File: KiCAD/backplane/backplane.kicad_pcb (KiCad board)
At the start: 2 copper layers, 121.9 x 88.9 mm, 37 parts, among them P1 CONN_02X04, P10 CONN_02X04, P11 CONN_01X09, P12 CONN_02X04, P13 CONN_01X09, P14 CONN_01X10, P15 CONN_01X10, P16 CONN_02X04, P17 CONN_02X04, P18 CONN_02X04, P19 CONN_01X09, P2 CONN_01X17, P20 CONN_01X04, P21 CONN_01X02, P22 CONN_01X02, P23 CONN_01X02, P3 CONN_01X17, P4 CONN_01X04, P5 CONN_01X09, P6 CONN_02X04, P7 CONN_01X10, P8 CONN_01X10, P9 CONN_02X04, U1 ARDUINO_MICRO

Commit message: switch adapter board mounting
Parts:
- added P24: CONN_01X01, myparts:4994-0-15-15-11-27-10-0, F.Cu at (28.5, -54.6)
- added P25: CONN_01X01, myparts:4994-0-15-15-11-27-10-0, F.Cu at (28.5, -52.1)
- added P26: CONN_01X01, myparts:4994-0-15-15-11-27-10-0, F.Cu at (28.5, -49.5)
- added P27: CONN_01X01, myparts:4994-0-15-15-11-27-10-0, F.Cu at (28.5, -47.0)
- added P28: CONN_01X01, myparts:4994-0-15-15-11-27-10-0, F.Cu at (28.5, -44.5)
- added P29: CONN_01X01, myparts:4994-0-15-15-11-27-10-0, F.Cu at (28.5, -41.9)
- added P30: CONN_01X01, myparts:4994-0-15-15-11-27-10-0, F.Cu at (28.5, -39.4)
- added P31: CONN_01X01, myparts:4994-0-15-15-11-27-10-0, F.Cu at (28.5, -36.8)
- added P32: CONN_01X01, myparts:4994-0-15-15-11-27-10-0, F.Cu at (28.5, -34.3)
- added P33: CONN_01X01, myparts:4994-0-15-15-11-27-10-0, F.Cu at (56.0, -52.1)
- added P34: CONN_01X01, myparts:4994-0-15-15-11-27-10-0, F.Cu at (56.0, -39.4)
- added P35: CONN_01X01, myparts:4994-0-15-15-11-27-10-0, F.Cu at (56.0, -47.0)
- added P36: CONN_01X01, myparts:4994-0-15-15-11-27-10-0, F.Cu at (56.0, -49.5)
- added P37: CONN_01X01, myparts:4994-0-15-15-11-27-10-0, F.Cu at (56.0, -41.9)
- added P38: CONN_01X01, myparts:4994-0-15-15-11-27-10-0, F.Cu at (96.0, -44.5)
- added P39: CONN_01X01, myparts:4994-0-15-15-11-27-10-0, F.Cu at (68.5, -44.5)
- added P40: CONN_01X01, myparts:4994-0-15-15-11-27-10-0, F.Cu at (56.0, -34.3)
- added P41: CONN_01X01, myparts:4994-0-15-15-11-27-10-0, F.Cu at (68.5, -54.6)
- added P42: CONN_01X01, myparts:4994-0-15-15-11-27-10-0, F.Cu at (68.5, -52.1)
- added P43: CONN_01X01, myparts:4994-0-15-15-11-27-10-0, F.Cu at (68.5, -49.5)
- added P44: CONN_01X01, myparts:4994-0-15-15-11-27-10-0, F.Cu at (68.5, -47.0)
- added P45: CONN_01X01, myparts:4994-0-15-15-11-27-10-0, F.Cu at (68.5, -39.4)
- added P46: CONN_01X01, myparts:4994-0-15-15-11-27-10-0, F.Cu at (68.5, -41.9)
- added P47: CONN_01X01, myparts:4994-0-15-15-11-27-10-0, F.Cu at (96.0, -49.5)
- added P48: CONN_01X01, myparts:4994-0-15-15-11-27-10-0, F.Cu at (68.5, -36.8)
- added P49: CONN_01X01, myparts:4994-0-15-15-11-27-10-0, F.Cu at (68.5, -34.3)
- added P50: CONN_01X01, myparts:4994-0-15-15-11-27-10-0, F.Cu at (56.0, -54.6)
- added P51: CONN_01X01, myparts:4994-0-15-15-11-27-10-0, F.Cu at (96.0, -52.1)
- added P52: CONN_01X01, myparts:4994-0-15-15-11-27-10-0, F.Cu at (96.0, -39.4)
- added P53: CONN_01X01, myparts:4994-0-15-15-11-27-10-0, F.Cu at (96.0, -47.0)
- added P54: CONN_01X01, myparts:4994-0-15-15-11-27-10-0, F.Cu at (96.0, -36.8)
- added P55: CONN_01X01, myparts:4994-0-15-15-11-27-10-0, F.Cu at (96.0, -41.9)
- added P56: CONN_01X01, myparts:4994-0-15-15-11-27-10-0, F.Cu at (56.0, -44.5)
- added P57: CONN_01X01, myparts:4994-0-15-15-11-27-10-0, F.Cu at (56.0, -36.8)
- added P58: CONN_01X01, myparts:4994-0-15-15-11-27-10-0, F.Cu at (96.0, -34.3)
- added P59: CONN_01X01, myparts:4994-0-15-15-11-27-10-0, F.Cu at (38.4, -30.7)
- added P60: CONN_01X01, myparts:4994-0-15-15-11-27-10-0, F.Cu at (41.0, -58.2)
- added P61: CONN_01X01, myparts:4994-0-15-15-11-27-10-0, F.Cu at (41.0, -30.7)
- added P62: CONN_01X01, myparts:4994-0-15-15-11-27-10-0, F.Cu at (43.5, -58.2)
- added P63: CONN_01X01, myparts:4994-0-15-15-11-27-10-0, F.Cu at (43.5, -30.7)
- added P64: CONN_01X01, myparts:4994-0-15-15-11-27-10-0, F.Cu at (88.6, -58.2)
- added P65: CONN_01X01, myparts:4994-0-15-15-11-27-10-0, F.Cu at (46.0, -30.7)
- added P66: CONN_01X01, myparts:4994-0-15-15-11-27-10-0, F.Cu at (46.0, -58.2)
- added P67: CONN_01X01, myparts:4994-0-15-15-11-27-10-0, F.Cu at (48.6, -30.7)
- added P68: CONN_01X01, myparts:4994-0-15-15-11-27-10-0, F.Cu at (51.1, -58.2)
- added P69: CONN_01X01, myparts:4994-0-15-15-11-27-10-0, F.Cu at (51.1, -30.7)
- added P70: CONN_01X01, myparts:4994-0-15-15-11-27-10-0, F.Cu at (53.7, -58.2)
- added P71: CONN_01X01, myparts:4994-0-15-15-11-27-10-0, F.Cu at (53.7, -30.7)
- added P72: CONN_01X01, myparts:4994-0-15-15-11-27-10-0, F.Cu at (70.8, -58.2)
- added P73: CONN_01X01, myparts:4994-0-15-15-11-27-10-0, F.Cu at (70.8, -30.7)
- added P74: CONN_01X01, myparts:4994-0-15-15-11-27-10-0, F.Cu at (73.3, -58.2)
- added P75: CONN_01X01, myparts:4994-0-15-15-11-27-10-0, F.Cu at (73.3, -30.7)
- added P76: CONN_01X01, myparts:4994-0-15-15-11-27-10-0, F.Cu at (75.9, -58.2)
- added P77: CONN_01X01, myparts:4994-0-15-15-11-27-10-0, F.Cu at (75.9, -30.7)
- added P78: CONN_01X01, myparts:4994-0-15-15-11-27-10-0, F.Cu at (86.0, -58.2)
- added P79: CONN_01X01, myparts:4994-0-15-15-11-27-10-0, F.Cu at (78.4, -30.7)
- added P80: CONN_01X01, myparts:4994-0-15-15-11-27-10-0, F.Cu at (81.0, -58.2)
- added P81: CONN_01X01, myparts:4994-0-15-15-11-27-10-0, F.Cu at (81.0, -30.7)
- added P82: CONN_01X01, myparts:4994-0-15-15-11-27-10-0, F.Cu at (83.5, -58.2)
- added P83: CONN_01X01, myparts:4994-0-15-15-11-27-10-0, F.Cu at (83.5, -30.7)
- added P84: CONN_01X01, myparts:4994-0-15-15-11-27-10-0, F.Cu at (38.4, -58.2)
- added P85: CONN_01X01, myparts:4994-0-15-15-11-27-10-0, F.Cu at (86.0, -30.7)
- added P86: CONN_01X01, myparts:4994-0-15-15-11-27-10-0, F.Cu at (35.9, -58.2)
- added P87: CONN_01X01, myparts:4994-0-15-15-11-27-10-0, F.Cu at (88.6, -30.7)
- added P88: CONN_01X01, myparts:4994-0-15-15-11-27-10-0, F.Cu at (91.1, -58.2)
- added P89: CONN_01X01, myparts:4994-0-15-15-11-27-10-0, F.Cu at (91.1, -30.7)
- added P90: CONN_01X01, myparts:4994-0-15-15-11-27-10-0, F.Cu at (93.7, -58.2)
- added P91: CONN_01X01, myparts:4994-0-15-15-11-27-10-0, F.Cu at (93.7, -30.7)
- P11, P13, P19, P5: value CONN_01X09 -> CONN_01X01; footprint Socket_Strips:Socket_Strip_Straight_1x09 -> myparts:4994-0-15-15-11-27-10-0
- P14, P15, P7, P8: value CONN_01X10 -> CONN_01X01; footprint Socket_Strips:Socket_Strip_Straight_1x10 -> myparts:4994-0-15-15-11-27-10-0
- moved P13 67.5 mm to (96.0, -54.6), turned to 90 degrees
- moved P11 67.0 mm to (33.3, -30.7), turned to 0 degrees
- moved P7 48.5 mm to (30.8, -30.7)
- moved P8 46.4 mm to (33.3, -58.2)
- moved P5 37.9 mm to (30.8, -58.2), turned to 0 degrees
- moved P19 22.7 mm to (78.4, -58.2), turned to 0 degrees
- moved P14 17.8 mm to (48.6, -58.2)
- moved P15 5.08 mm to (35.9, -30.7)
- renumbered JTAG to CON1
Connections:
- P11 pad 1: +5V -> B1_V
- P13 pad 1: MOSI -> +5V
- P14 pad 1: B0_I -> (no net)
- P15 pad 1: B1_I -> B_I+
- P19 pad 1: +5V -> (no net)
- P5 pad 1: MOSI -> B0_I
- P7 pad 1: A0_I -> B1_I
- P8 pad 1: A1_I -> B0_V
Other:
- board text added: "JTAG"

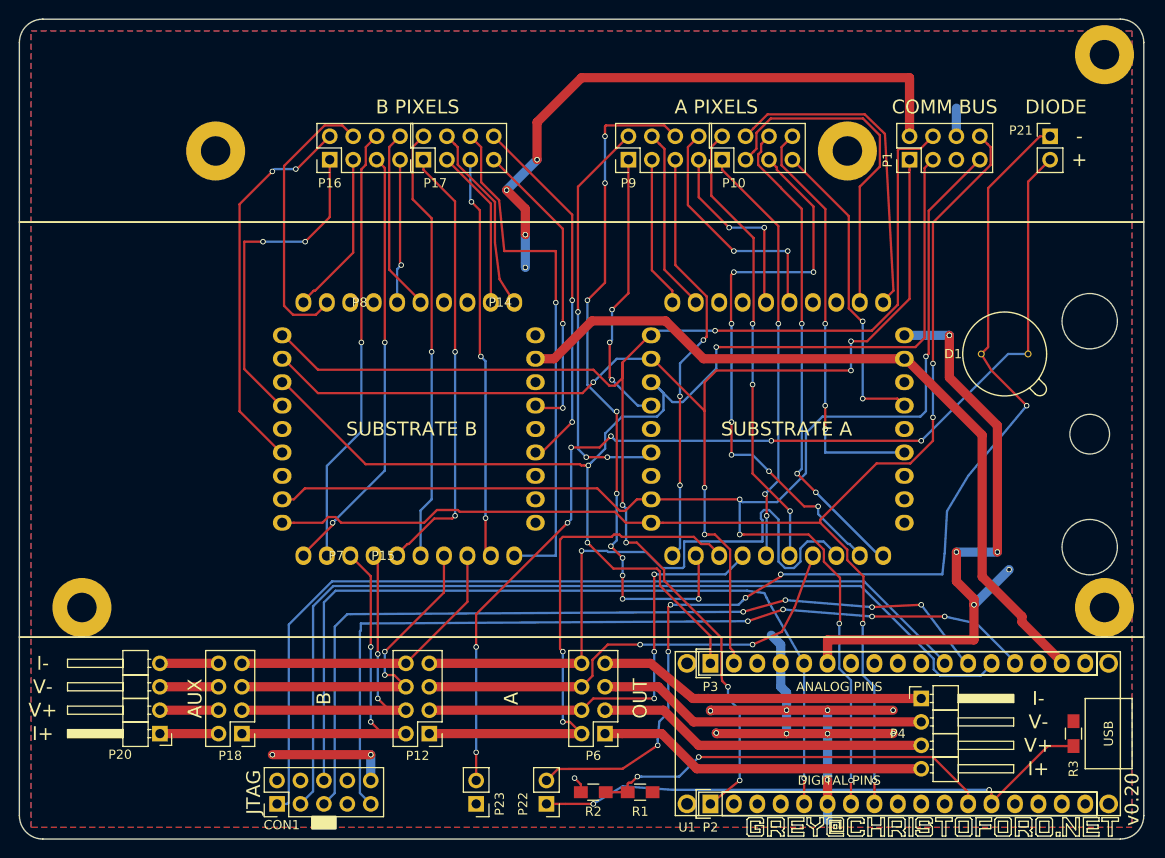
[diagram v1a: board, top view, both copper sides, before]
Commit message: properly link mounting holes to schematic
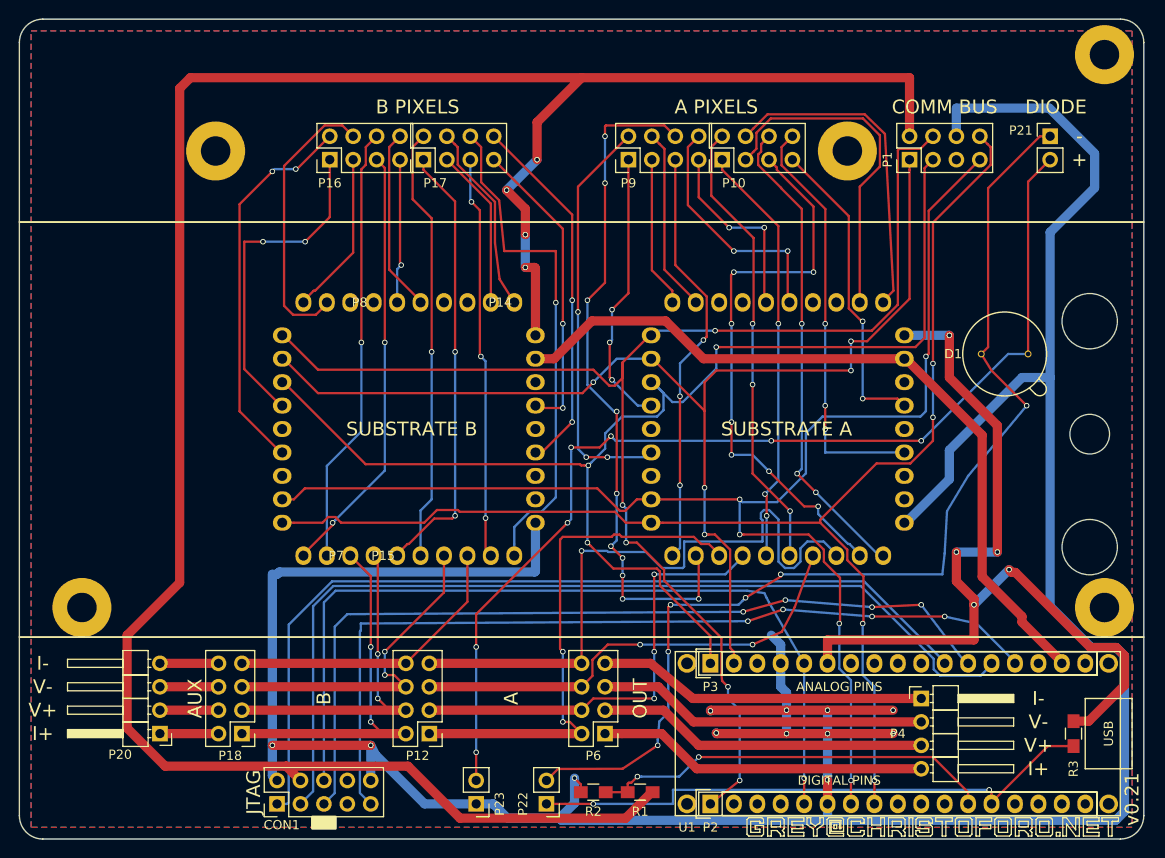
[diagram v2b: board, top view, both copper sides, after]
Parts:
- P92, P96, P97, P98, P99: renamed from REF**; value MountingHole_3.2mm_M3_Pad -> CONN_01X01
- P93, P95: renamed from REF**; value MountingHole_6mm -> CONN_01X01
- P94: renamed from REF**; value MountingHole_4.3mm_M4 -> CONN_01X01
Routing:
- net GND: track 81.0 -> 348.7 mm
- net +5V: track 135.8 -> 351.1 mm
- net B5_V: track 56.9 -> 55.0 mm
- net ADC11: track 61.8 -> 62.7 mm
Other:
- board text added: "v0.21"
- board text removed: "v0.20"

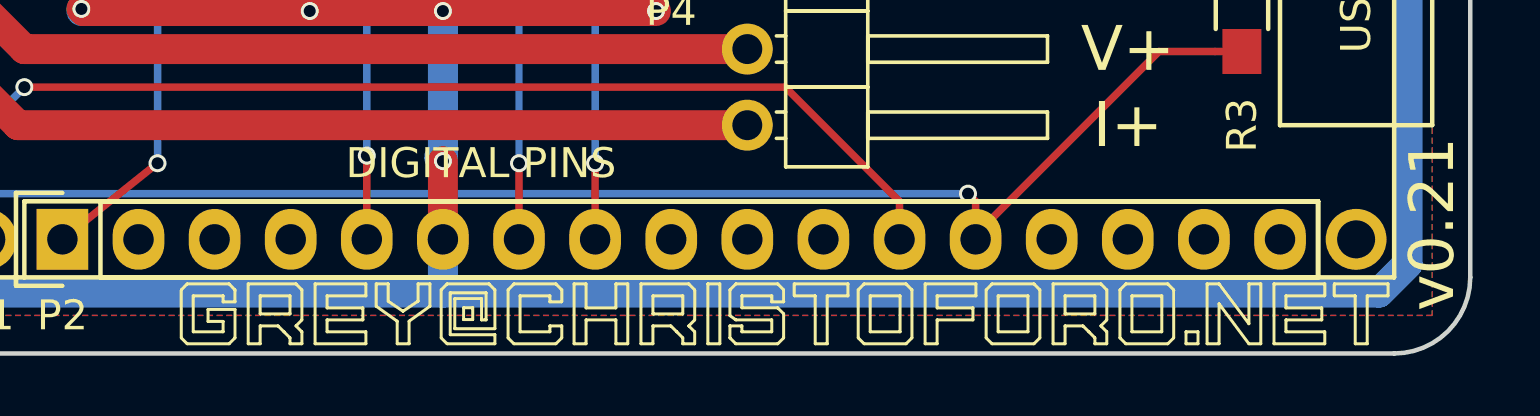
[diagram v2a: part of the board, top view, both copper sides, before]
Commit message: 28x28 mux adapter done28x28 mux adapter done
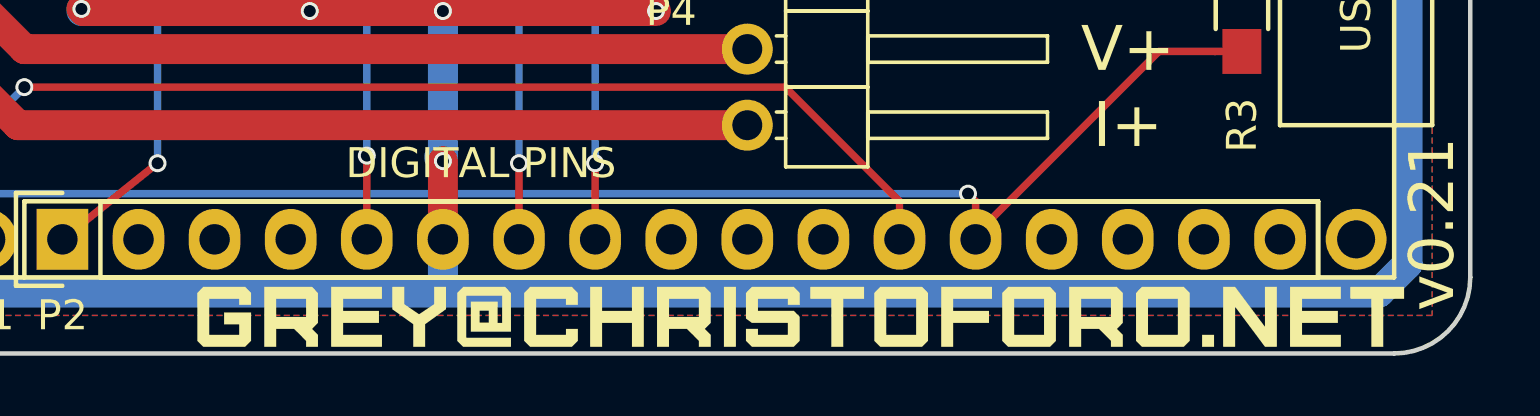
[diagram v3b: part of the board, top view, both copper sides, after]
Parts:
- added G***: value, myparts:logo, F.Cu at (99.6, -1.20)

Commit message: fix up some hardware bugs
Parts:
- added R4: 10K, Resistors_SMD:R_0805_HandSoldering, B.Cu at (91.5, -14.0)
- added R5: 10K, Resistors_SMD:R_0805_HandSoldering, B.Cu at (96.0, -15.5)
- R3: value 1M -> 2k
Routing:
- net SCL: track 145.2 -> 148.9 mm
- net +5V: track 351.1 -> 352.9 mm, vias 9 -> 11
- net SDA: track 150.7 -> 152.1 mm
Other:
- board text added: "v0.22"
- board text removed: "v0.21"
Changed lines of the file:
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@@
 (kicad_pcb (version 4) (host pcbnew 4.0.5)
   (general
-    (links 0)
+    (links 105)
     (no_connects 0)
-    (area -0.100001 -90.223 122.690334 0.358095)
+    (area -0.075001 -88.975001 121.995001 0.075001)
     (thickness 1.6)
     (drawings 32)
-    (tracks 899)
+    (tracks 911)
     (zones 0)
-    (modules 106)
+    (modules 108)
     (nets 66)
   )
@@
     (39 F.Mask user)
     (40 Dwgs.User user)
-    (41 Cmts.User user hide)
-    (42 Eco1.User user hide)
-    (43 Eco2.User user hide)
+    (41 Cmts.User user)
+    (42 Eco1.User user)
+    (43 Eco2.User user)
     (44 Edge.Cuts user)
     (45 Margin user)
-    (46 B.CrtYd user hide)
-    (47 F.CrtYd user hide)
+    (46 B.CrtYd user)
+    (47 F.CrtYd user)
     (48 B.Fab user hide)
     (49 F.Fab user hide)
@@
     (pad_to_mask_clearance 0.2)
     (aux_axis_origin 0 0)
-    (visible_elements FFFFFF3F)
+    (visible_elements FFFFFF7F)
     (pcbplotparams
       (layerselection 0x010fc_80000001)
@@
       (effects (font (size 1 1) (thickness 0.15)))
     )
-    (fp_text value 1M (at 0 2.1 270) (layer F.Fab)
+    (fp_text value 2k (at 0 2.1 270) (layer F.Fab)
       (effects (font (size 1 1) (thickness 0.15)))
     )
@@
       (xy 8.293997 0.976563) (xy 8.491005 0.779554)) (layer F.SilkS) (width 0.001))
   )
+  (module Resistors_SMD:R_0805_HandSoldering (layer B.Cu)
+    (at 91.5 -14 270)
+    (descr "Resistor SMD 0805, hand soldering")
+    (tags "resistor 0805")
+    (attr smd)
+    (fp_text reference R4 (at 0 2 270) (layer B.SilkS)
+      (effects (font (size 1 1) (thickness 0.15)) (justify mirror))
+    )
+    (fp_text value 10K (at 0 -2.1 270) (layer B.Fab)
+      (effects (font (size 1 1) (thickness 0.15)) (justify mirror))
+    )
+    (fp_line (start -1 -0.625) (end -1 0.625) (layer B.Fab) (width 0.1))
+    (fp_line (start 1 -0.625) (end -1 -0.625) (layer B.Fab) (width 0.1))
+    (fp_line (start 1 0.625) (end 1 -0.625) (layer B.Fab) (width 0.1))
+    (fp_line (start -1 0.625) (end 1 0.625) (layer B.Fab) (width 0.1))
+    (fp_line (start -2.4 1) (end 2.4 1) (layer B.CrtYd) (width 0.05))
+    (fp_line (start -2.4 -1) (end 2.4 -1) (layer B.CrtYd) (width 0.05))
+    (fp_line (start -2.4 1) (end -2.4 -1) (layer B.CrtYd) (width 0.05))
+    (fp_line (start 2.4 1) (end 2.4 -1) (layer B.CrtYd) (width 0.05))
+    (fp_line (start 0.6 -0.875) (end -0.6 -0.875) (layer B.SilkS) (width 0.15))
+    (fp_line (start -0.6 0.875) (end 0.6 0.875) (layer B.SilkS) (width 0.15))
+    (pad 1 smd rect (at -1.35 0 270) (size 1.5 1.3) (layers B.Cu B.Paste B.Mask)
+      (net 2 +5V))
+    (pad 2 smd rect (at 1.35 0 270) (size 1.5 1.3) (layers B.Cu B.Paste B.Mask)
+      (net 6 SDA))
+    (model Resistors_SMD.3dshapes/R_0805_HandSoldering.wrl
+      (at (xyz 0 0 0))
+      (scale (xyz 1 1 1))
+      (rotate (xyz 0 0 0))
+    )
+  )
+  (module Resistors_SMD:R_0805_HandSoldering (layer B.Cu)
+    (at 96 -15.5 270)
+    (descr "Resistor SMD 0805, hand soldering")
+    (tags "resistor 0805")
+    (attr smd)
+    (fp_text reference R5 (at -1.5 1.5 270) (layer B.SilkS)
+      (effects (font (size 1 1) (thickness 0.15)) (justify mirror))
+    )
+    (fp_text value 10K (at 0 -2.1 270) (layer B.Fab)
+      (effects (font (size 1 1) (thickness 0.15)) (justify mirror))
+    )
+    (fp_line (start -1 -0.625) (end -1 0.625) (layer B.Fab) (width 0.1))
+    (fp_line (start 1 -0.625) (end -1 -0.625) (layer B.Fab) (width 0.1))
+    (fp_line (start 1 0.625) (end 1 -0.625) (layer B.Fab) (width 0.1))
+    (fp_line (start -1 0.625) (end 1 0.625) (layer B.Fab) (width 0.1))
+    (fp_line (start -2.4 1) (end 2.4 1) (layer B.CrtYd) (width 0.05))
+    (fp_line (start -2.4 -1) (end 2.4 -1) (layer B.CrtYd) (width 0.05))
+    (fp_line (start -2.4 1) (end -2.4 -1) (layer B.CrtYd) (width 0.05))
+    (fp_line (start 2.4 1) (end 2.4 -1) (layer B.CrtYd) (width 0.05))
+    (fp_line (start 0.6 -0.875) (end -0.6 -0.875) (layer B.SilkS) (width 0.15))
+    (fp_line (start -0.6 0.875) (end 0.6 0.875) (layer B.SilkS) (width 0.15))
+    (pad 1 smd rect (at -1.35 0 270) (size 1.5 1.3) (layers B.Cu B.Paste B.Mask)
+      (net 2 +5V))
+    (pad 2 smd rect (at 1.35 0 270) (size 1.5 1.3) (layers B.Cu B.Paste B.Mask)
+      (net 7 SCL))
+    (model Resistors_SMD.3dshapes/R_0805_HandSoldering.wrl
+      (at (xyz 0 0 0))
+      (scale (xyz 1 1 1))
+      (rotate (xyz 0 0 0))
+    )
+  )
   (gr_text JTAG (at 25.4 -5.08 90) (layer F.SilkS)
     (effects (font (size 1.5 1.5) (thickness 0.3)))
   )
-  (gr_text v0.21 (at 120.65 -4.318 90) (layer F.SilkS)
+  (gr_text v0.22 (at 120.65 -4.318 90) (layer F.SilkS)
     (effects (font (size 1.5 1.5) (thickness 0.3)))
   )
@@
   (gr_line (start 0 -66.9) (end 121.92 -66.9) (layer F.SilkS) (width 0.2))
   (gr_line (start 0 -21.9) (end 121.92 -21.9) (layer F.SilkS) (width 0.2))
-  (gr_text "COMM BUS" (at 100.33 -79.375) (layer F.SilkS)
+  (gr_text "COMM BUS" (at 100.33 -78.5) (layer F.SilkS)
     (effects (font (size 1.5 1.5) (thickness 0.3)))
   )
@@
   (via (at 74.295 -38.1) (size 0.6) (drill 0.4) (layers F.Cu B.Cu) (net 1))
   (via (at 74.295 -33.02) (size 0.6) (drill 0.4) (layers F.Cu B.Cu) (net 1))
+  (segment (start 91.5 -15.35) (end 91.5 -16.5) (width 0.25) (layer B.Cu) (net 2))
+  (segment (start 91.5 -16.5) (end 91 -17) (width 0.25) (layer B.Cu) (net 2))
+  (via (at 91 -17) (size 0.6) (drill 0.4) (layers F.Cu B.Cu) (net 2))
+  (via (at 96 -16.85) (size 0.6) (drill 0.4) (layers F.Cu B.Cu) (net 2))
   (segment (start 68.66 -5.08) (end 68.56 -5.08) (width 1) (layer F.Cu) (net 2))
   (segment (start 68.56 -5.08) (end 65.739999 -2.259999) (width 1) (layer F.Cu) (net 2))
@@
   (segment (start 60.88 -5.922) (end 60.198 -6.604) (width 0.25) (layer F.Cu) (net 5))
   (via (at 60.198 -6.604) (size 0.6) (drill 0.4) (layers F.Cu B.Cu) (net 5))
+  (segment (start 90.17 -6.35) (end 90.17 -12.5) (width 0.25) (layer B.Cu) (net 6))
+  (segment (start 90.17 -12.5) (end 90.17 -16.51) (width 0.25) (layer B.Cu) (net 6))
+  (segment (start 91.5 -12.65) (end 90.6 -12.65) (width 0.25) (layer B.Cu) (net 6))
+  (segment (start 90.6 -12.65) (end 90.45 -12.5) (width 0.25) (layer B.Cu) (net 6))
+  (segment (start 90.45 -12.5) (end 90.17 -12.5) (width 0.25) (layer B.Cu) (net 6))
   (segment (start 78.404999 -36.530001) (end 78.105 -36.83) (width 0.25) (layer B.Cu) (net 6))
   (segment (start 85.286011 -39.657007) (end 82.159005 -36.530001) (width 0.25) (layer B.Cu) (net 6))
@@
   (via (at 78.105 -36.83) (size 0.6) (drill 0.4) (layers F.Cu B.Cu) (net 6))
   (via (at 78.105 -33.02) (size 0.6) (drill 0.4) (layers F.Cu B.Cu) (net 6))
-  (segment (start 90.17 -6.35) (end 90.17 -16.51) (width 0.25) (layer B.Cu) (net 6))
   (segment (start 90.17 -3.81) (end 90.17 -6.35) (width 0.25) (layer F.Cu) (net 6))
   (via (at 90.17 -6.35) (size 0.6) (drill 0.4) (layers F.Cu B.Cu) (net 6))
+  (segment (start 92.71 -6.35) (end 92.71 -15) (width 0.25) (layer B.Cu) (net 7))
+  (segment (start 92.71 -15) (end 92.71 -16.51) (width 0.25) (layer B.Cu) (net 7))
+  (segment (start 96 -14.15) (end 96 -14.25) (width 0.25) (layer B.Cu) (net 7))
+  (segment (start 96 -14.25) (end 95.25 -15) (width 0.25) (layer B.Cu) (net 7))
+  (segment (start 95.25 -15) (end 92.71 -15) (width 0.25) (layer B.Cu) (net 7))
   (segment (start 29.766 -34.295) (end 28.5 -34.295) (width 0.25) (layer F.Cu) (net 7))
   (segment (start 32.861998 -34.295) (end 29.766 -34.295) (width 0.25) (layer F.Cu) (net 7))
@@
   (segment (start 86.843348 -34.295) (end 69.766 -34.295) (width 0.25) (layer F.Cu) (net 7))
   (segment (start 69.766 -34.295) (end 68.5 -34.295) (width 0.25) (layer F.Cu) (net 7))
-  (segment (start 92.71 -6.35) (end 92.71 -16.51) (width 0.25) (layer B.Cu) (net 7))
   (segment (start 92.71 -3.81) (end 92.71 -6.35) (width 0.25) (layer F.Cu) (net 7))
   (via (at 92.71 -6.35) (size 0.6) (drill 0.4) (layers F.Cu B.Cu) (net 7))
